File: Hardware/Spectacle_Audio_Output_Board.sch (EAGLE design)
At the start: 77 parts, among them J3 Audio Jack, J4 AUDIO-JACK3, J5 AUDIO-JACK3, U1 CY8C4146LQI-S422, U2 3.3V, U3 3.3V, U4 AT25SF041-SOIC8, Y1 12MHz

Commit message: Submitted for review by QC
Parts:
- added C11: 10uF, SparkFun-Capacitors:10UF-6.3V-20%(0603)
- added FD5, FD6, FD7, FD8: FIDUCIALUFIDUCIAL, SparkFun-Aesthetics:FIDUCIALUFIDUCIAL
- added R2: 1M, SparkFun-Resistors:1MOHM-1/10W-1%(0603)
- J3: value Audio Jack -> (none); device SparkFun-Connectors:AUDIO-JACKSMD -> SparkFun-Connectors:AUDIO-JACKSMD2
- renumbered U$2 to U5
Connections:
- new net VCCIO: C12.1, R11.2, R12.2, R13.2, R14.2, R15.2, R16.2, R17.2, R29.2, U5.IOVDD1, U5.IOVDD2, U5.IOVDD3
- new net VDDA: C11.1, U5.AVDD1, U5.AVDD2, U5.AVDD3, U5.AVDD4
- net 3.3V: now also C21.2; no longer C12.1, R11.2, R12.2, R13.2, R14.2, R15.2, R16.2, R17.2, R26.1, R29.2, U5.AVDD1, U5.AVDD2, U5.AVDD3, U5.AVDD4, U5.IOVDD1, U5.IOVDD2, U5.IOVDD3
- net GND: now also C11.2, R2.2, R26.2; no longer C21.1
- net N$12: now also R2.1
- net N$15: now also C21.1, R26.1; no longer C21.2, R26.2
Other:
- note added: "4.5V < VIN < 5.5V"
- note added: "I2C Pullup Disable"
- moved on the sheet: C21, J3, R26

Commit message: Fixes from QC review
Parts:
- renumbered C22 to C20, D5 to D1
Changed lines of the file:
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@@
 <part name="D4" library="SparkFun-DiscreteSemi" deviceset="PESD1CAN" device=""/>
 <part name="GND4" library="SparkFun-Aesthetics" deviceset="GND" device=""/>
-<part name="D5" library="SparkFun-DiscreteSemi" deviceset="PESD1CAN" device=""/>
+<part name="D1" library="SparkFun-DiscreteSemi" deviceset="PESD1CAN" device=""/>
 <part name="SUPPLY1" library="SparkFun-Aesthetics" deviceset="3.3V" device=""/>
 <part name="H1" library="SparkFun-Electromechanical" deviceset="STAND-OFF" device=""/>
@@
 <part name="GND28" library="SparkFun-Aesthetics" deviceset="GND" device=""/>
 <part name="R29" library="SparkFun-Resistors" deviceset="100KOHM-1/16W-1%(0402)" device="" value="100K"/>
-<part name="C22" library="SparkFun-Capacitors" deviceset="2.2UF-10V-20%(0603)" device="" value="2.2uF"/>
+<part name="C20" library="SparkFun-Capacitors" deviceset="2.2UF-10V-20%(0603)" device="" value="2.2uF"/>
 <part name="C12" library="SparkFun-Capacitors" deviceset="10UF-6.3V-20%(0603)" device="" value="10uF"/>
 <part name="C9" library="SparkFun-Capacitors" deviceset="0.1UF-16V(+-10%)(0402)" device="" value="0.1uF"/>
@@
 <instance part="D4" gate="G$1" x="223.52" y="71.12" rot="MR180"/>
 <instance part="GND4" gate="1" x="241.3" y="40.64"/>
-<instance part="D5" gate="G$1" x="223.52" y="43.18"/>
+<instance part="D1" gate="G$1" x="223.52" y="43.18"/>
 <instance part="SUPPLY1" gate="G$1" x="22.86" y="177.8"/>
 <instance part="H1" gate="G$1" x="246.38" y="33.02"/>
@@
 <wire x1="238.76" y1="66.04" x2="241.3" y2="66.04" width="0.1524" layer="91"/>
 <wire x1="241.3" y1="66.04" x2="241.3" y2="48.26" width="0.1524" layer="91"/>
-<pinref part="D5" gate="G$1" pin="3"/>
+<pinref part="D1" gate="G$1" pin="3"/>
 <wire x1="241.3" y1="48.26" x2="241.3" y2="43.18" width="0.1524" layer="91"/>
 <wire x1="238.76" y1="48.26" x2="241.3" y2="48.26" width="0.1524" layer="91"/>
@@
 <wire x1="208.28" y1="45.72" x2="208.28" y2="48.26" width="0.1524" layer="91"/>
 <junction x="208.28" y="71.12"/>
-<pinref part="D5" gate="G$1" pin="2"/>
+<pinref part="D1" gate="G$1" pin="2"/>
 <wire x1="208.28" y1="48.26" x2="208.28" y2="71.12" width="0.1524" layer="91"/>
 <wire x1="208.28" y1="45.72" x2="218.44" y2="45.72" width="0.1524" layer="91"/>
@@
 <attribute name="VALUE" x="80.01" y="170.942" size="1.778" layer="96" rot="R180"/>
 </instance>
-<instance part="C22" gate="G$1" x="154.94" y="165.1"/>
+<instance part="C20" gate="G$1" x="154.94" y="165.1"/>
 <instance part="C12" gate="G$1" x="213.36" y="152.4"/>
 <instance part="C9" gate="G$1" x="223.52" y="152.4"/>
@@
 <pinref part="GND22" gate="1" pin="GND"/>
 <wire x1="154.94" y1="160.02" x2="154.94" y2="162.56" width="0.1524" layer="91"/>
-<pinref part="C22" gate="G$1" pin="2"/>
+<pinref part="C20" gate="G$1" pin="2"/>
 </segment>
 <segment>
@@
 <wire x1="154.94" y1="172.72" x2="152.4" y2="172.72" width="0.1524" layer="91"/>
 <junction x="152.4" y="172.72"/>
-<pinref part="C22" gate="G$1" pin="1"/>
-</segment>
-<segment>
+<pinref part="C20" gate="G$1" pin="1"/>
+</segment>
+<segment>

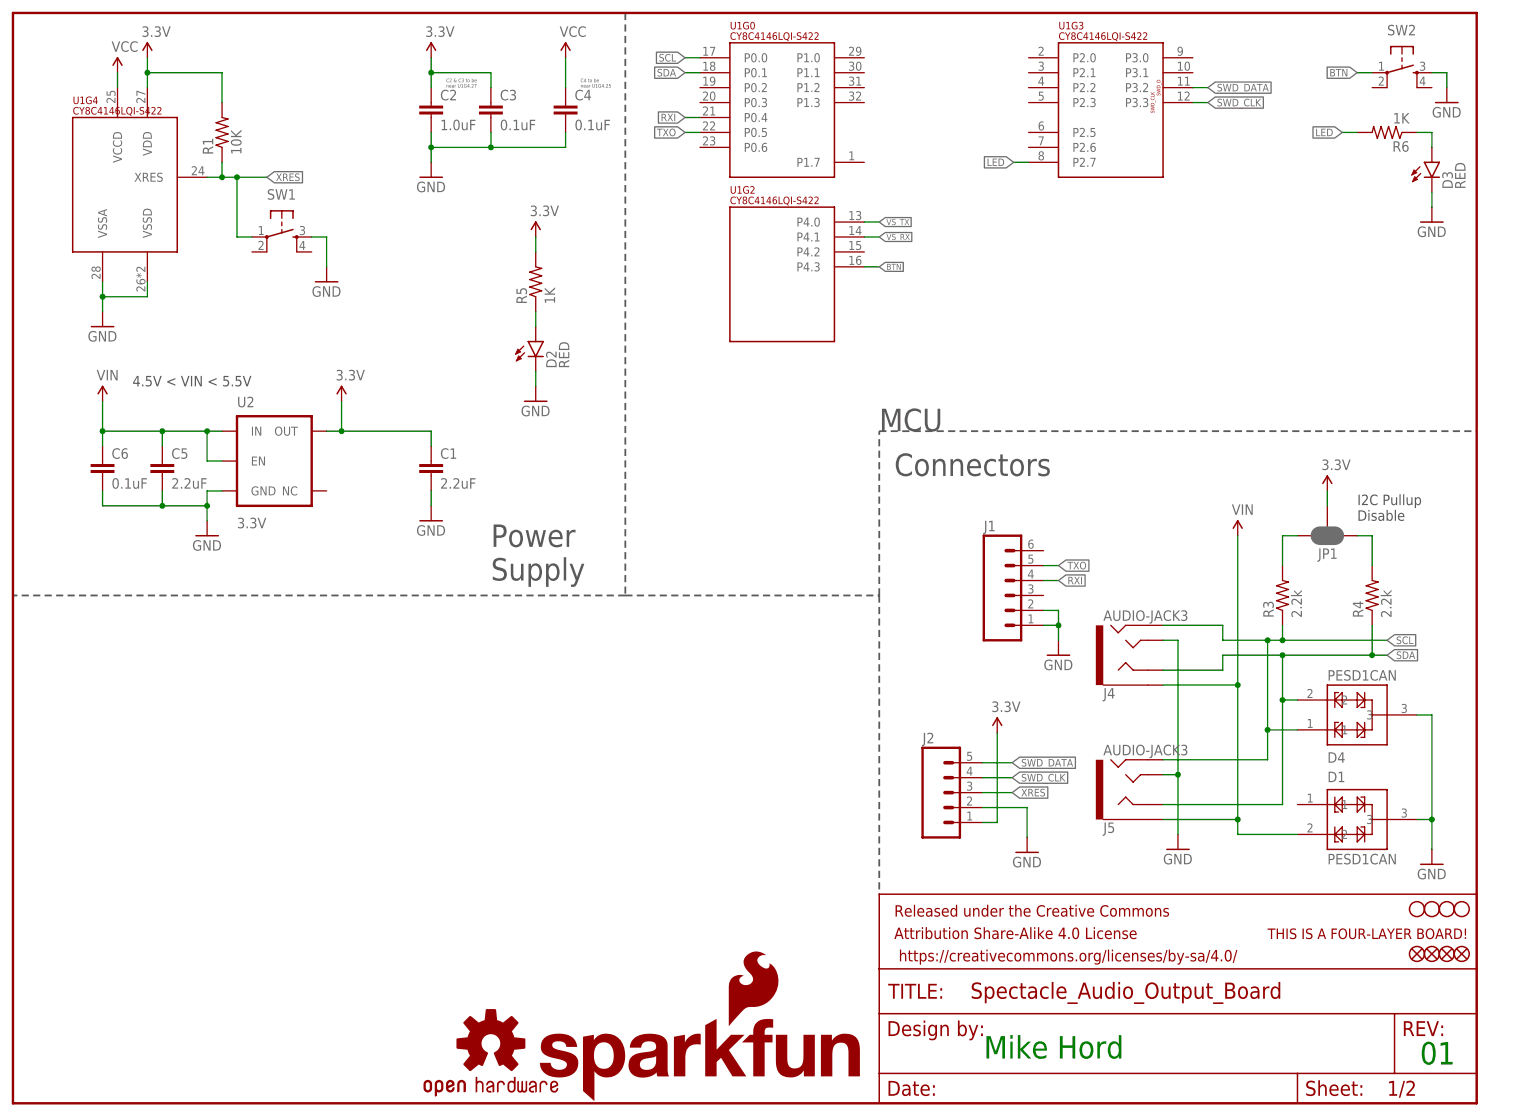
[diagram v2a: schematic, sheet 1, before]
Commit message: Added downstream power control circuitry
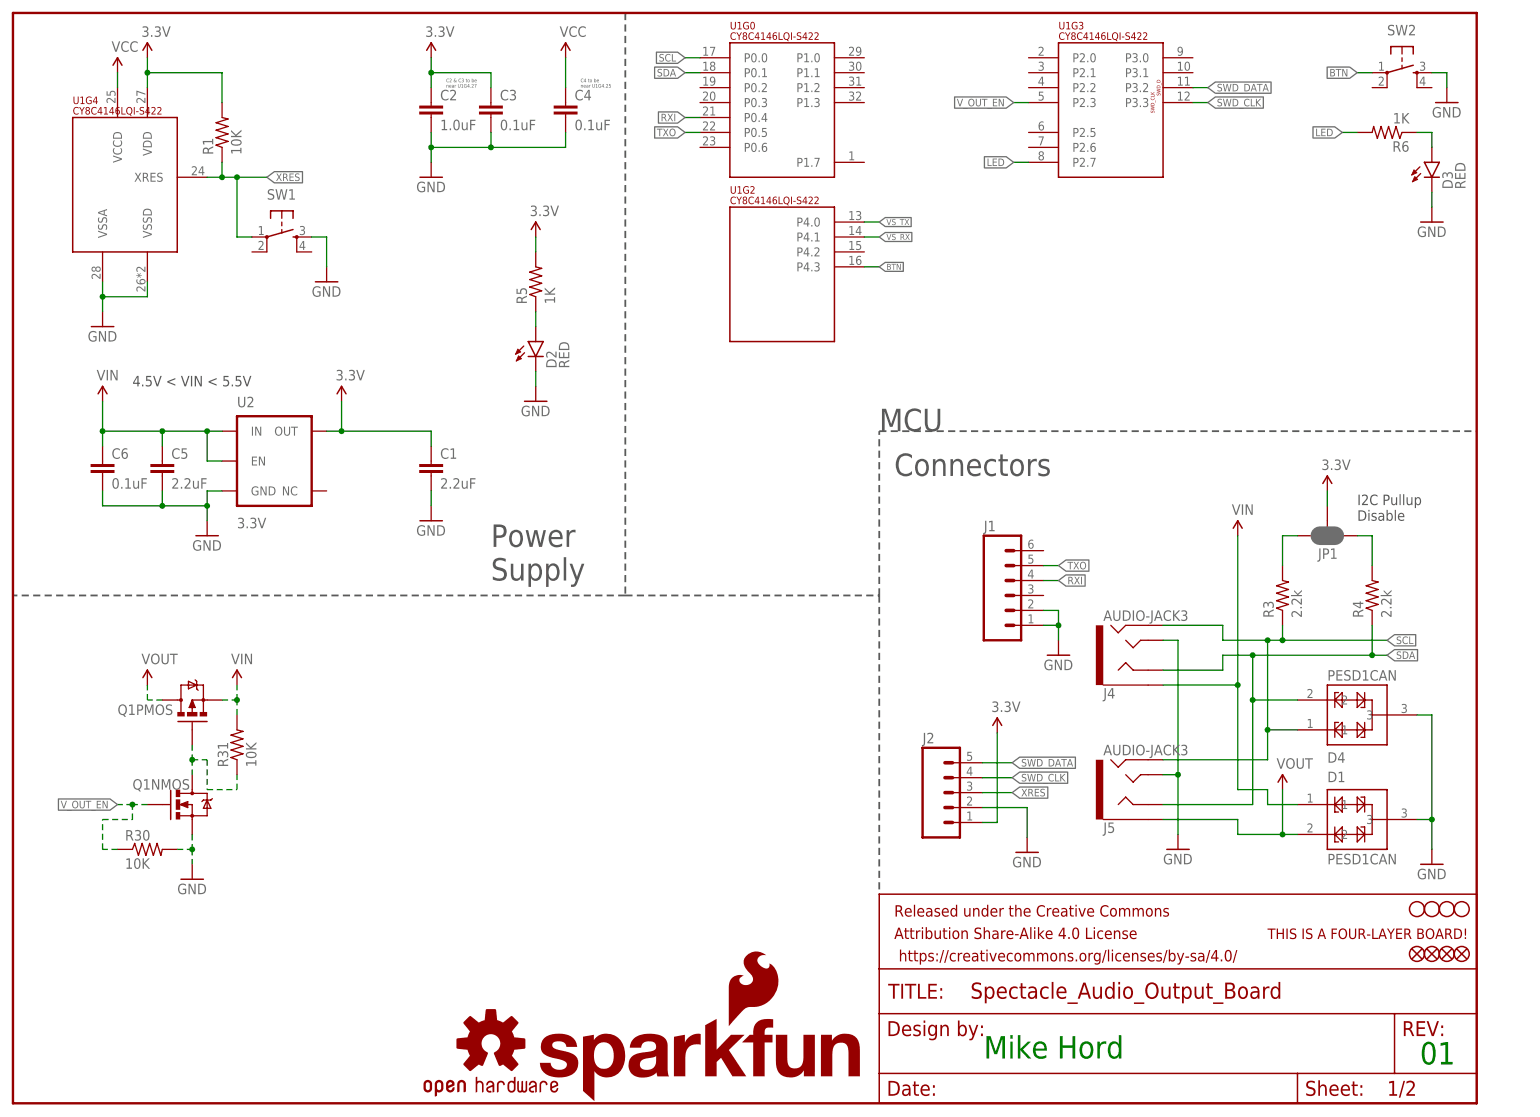
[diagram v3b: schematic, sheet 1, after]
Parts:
- added Q1: (no value), SparkFun-DiscreteSemi:IRF7509
- added R30, R31: 10K, SparkFun-Resistors:10KOHM-1/10W-1%(0603)0603
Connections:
- new net N$26: Q1NMOS.D, Q1PMOS.G, R31.1
- new net VOUT: D1.2, J5.EARTH, Q1PMOS.D
- new net V_OUT_EN: Q1NMOS.G, R30.1, U1G3.P2.3
- net GND: now also Q1NMOS.S, R30.2
- net VIN: now also D1.1, Q1PMOS.S, R31.2; no longer D1.2, J5.EARTH
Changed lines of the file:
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@@
 <part name="FD7" library="SparkFun-Aesthetics" deviceset="FIDUCIAL" device="UFIDUCIAL"/>
 <part name="FD8" library="SparkFun-Aesthetics" deviceset="FIDUCIAL" device="UFIDUCIAL"/>
+<part name="Q1" library="SparkFun-DiscreteSemi" deviceset="IRF7509" device=""/>
+<part name="GND30" library="SparkFun-Aesthetics" deviceset="GND" device=""/>
+<part name="SUPPLY23" library="SparkFun-Aesthetics" deviceset="VIN" device=""/>
+<part name="U$2" library="SparkFun-Aesthetics" deviceset="VOUT" device=""/>
+<part name="R30" library="SparkFun-Resistors" deviceset="10KOHM-1/10W-1%(0603)" device="0603" value="10K"/>
+<part name="R31" library="SparkFun-Resistors" deviceset="10KOHM-1/10W-1%(0603)" device="0603" value="10K"/>
+<part name="U$5" library="SparkFun-Aesthetics" deviceset="VOUT" device=""/>
 </parts>
 <sheets>
@@
 <instance part="FD7" gate="G$1" x="243.84" y="25.4"/>
 <instance part="FD8" gate="G$1" x="246.38" y="25.4"/>
+<instance part="Q1" gate="NMOS" x="30.48" y="50.8" smashed="yes">
+<attribute name="NAME" x="20.32" y="53.34" size="1.778" layer="95"/>
+<attribute name="VALUE" x="35.56" y="50.8" size="1.778" layer="96"/>
+</instance>
+<instance part="Q1" gate="PMOS" x="30.48" y="68.58" smashed="yes" rot="R90">
+<attribute name="NAME" x="17.78" y="66.04" size="1.778" layer="95"/>
+<attribute name="VALUE" x="30.48" y="73.66" size="1.778" layer="96" rot="R90"/>
+</instance>
+<instance part="GND30" gate="1" x="30.48" y="38.1"/>
+<instance part="SUPPLY23" gate="G$1" x="38.1" y="71.12"/>
+<instance part="U$2" gate="G$1" x="22.86" y="71.12"/>
+<instance part="R30" gate="G$1" x="22.86" y="43.18"/>
+<instance part="R31" gate="G$1" x="38.1" y="60.96" rot="R90"/>
+<instance part="U$5" gate="G$1" x="215.9" y="53.34"/>
 </instances>
 <busses>
@@
 <wire x1="238.76" y1="48.26" x2="241.3" y2="48.26" width="0.1524" layer="91"/>
 <junction x="241.3" y="48.26"/>
+</segment>
+<segment>
+<pinref part="Q1" gate="NMOS" pin="S"/>
+<pinref part="GND30" gate="1" pin="GND"/>
+<wire x1="30.48" y1="45.72" x2="30.48" y2="43.18" width="0.1524" layer="91" style="longdash"/>
+<pinref part="R30" gate="G$1" pin="2"/>
+<wire x1="30.48" y1="43.18" x2="30.48" y2="40.64" width="0.1524" layer="91" style="longdash"/>
+<wire x1="27.94" y1="43.18" x2="30.48" y2="43.18" width="0.1524" layer="91" style="longdash"/>
+<junction x="30.48" y="43.18"/>
 </segment>
 </net>
@@
 <wire x1="208.28" y1="71.12" x2="208.28" y2="96.52" width="0.1524" layer="91"/>
 <pinref part="J4" gate="G$1" pin="EARTH"/>
-<wire x1="208.28" y1="45.72" x2="208.28" y2="48.26" width="0.1524" layer="91"/>
+<wire x1="208.28" y1="71.12" x2="208.28" y2="53.34" width="0.1524" layer="91"/>
 <junction x="208.28" y="71.12"/>
-<pinref part="D1" gate="G$1" pin="2"/>
-<wire x1="208.28" y1="48.26" x2="208.28" y2="71.12" width="0.1524" layer="91"/>
-<wire x1="208.28" y1="45.72" x2="218.44" y2="45.72" width="0.1524" layer="91"/>
-<pinref part="J5" gate="G$1" pin="EARTH"/>
-<wire x1="195.58" y1="48.26" x2="208.28" y2="48.26" width="0.1524" layer="91"/>
-<junction x="208.28" y="48.26"/>
+<wire x1="208.28" y1="53.34" x2="213.36" y2="53.34" width="0.1524" layer="91"/>
+<wire x1="213.36" y1="53.34" x2="213.36" y2="50.8" width="0.1524" layer="91"/>
+<pinref part="D1" gate="G$1" pin="1"/>
+<wire x1="213.36" y1="50.8" x2="218.44" y2="50.8" width="0.1524" layer="91"/>
+</segment>
+<segment>
+<pinref part="Q1" gate="PMOS" pin="S"/>
+<wire x1="35.56" y1="68.58" x2="38.1" y2="68.58" width="0.1524" layer="91" style="longdash"/>
+<wire x1="38.1" y1="68.58" x2="38.1" y2="71.12" width="0.1524" layer="91" style="longdash"/>
+<pinref part="SUPPLY23" gate="G$1" pin="VIN"/>
+<pinref part="R31" gate="G$1" pin="2"/>
+<wire x1="38.1" y1="66.04" x2="38.1" y2="68.58" width="0.1524" layer="91" style="longdash"/>
+<junction x="38.1" y="68.58"/>
 </segment>
 </net>
@@
 <pinref part="R4" gate="G$1" pin="1"/>
 <wire x1="231.14" y1="81.28" x2="231.14" y2="76.2" width="0.1524" layer="91"/>
-<wire x1="231.14" y1="76.2" x2="215.9" y2="76.2" width="0.1524" layer="91"/>
-<wire x1="215.9" y1="76.2" x2="205.74" y2="76.2" width="0.1524" layer="91"/>
+<wire x1="231.14" y1="76.2" x2="210.82" y2="76.2" width="0.1524" layer="91"/>
+<wire x1="210.82" y1="76.2" x2="205.74" y2="76.2" width="0.1524" layer="91"/>
 <wire x1="231.14" y1="76.2" x2="233.68" y2="76.2" width="0.1524" layer="91"/>
 <junction x="231.14" y="76.2"/>
@@
 <pinref part="J4" gate="G$1" pin="RING1"/>
 <wire x1="205.74" y1="73.66" x2="195.58" y2="73.66" width="0.1524" layer="91"/>
-<wire x1="215.9" y1="68.58" x2="215.9" y2="76.2" width="0.1524" layer="91"/>
-<junction x="215.9" y="76.2"/>
+<wire x1="210.82" y1="68.58" x2="210.82" y2="76.2" width="0.1524" layer="91"/>
+<junction x="210.82" y="76.2"/>
 <pinref part="D4" gate="G$1" pin="2"/>
-<wire x1="218.44" y1="68.58" x2="215.9" y2="68.58" width="0.1524" layer="91"/>
+<wire x1="218.44" y1="68.58" x2="210.82" y2="68.58" width="0.1524" layer="91"/>
 <pinref part="J5" gate="G$1" pin="RING1"/>
-<wire x1="195.58" y1="50.8" x2="215.9" y2="50.8" width="0.1524" layer="91"/>
-<wire x1="215.9" y1="50.8" x2="215.9" y2="68.58" width="0.1524" layer="91"/>
-<junction x="215.9" y="68.58"/>
+<wire x1="195.58" y1="50.8" x2="210.82" y2="50.8" width="0.1524" layer="91"/>
+<wire x1="210.82" y1="50.8" x2="210.82" y2="68.58" width="0.1524" layer="91"/>
+<junction x="210.82" y="68.58"/>
 </segment>
 <segment>
@@
 </segment>
 </net>
+<net name="N$26" class="0">
+<segment>
+<pinref part="Q1" gate="PMOS" pin="G"/>
+<pinref part="Q1" gate="NMOS" pin="D"/>
+<wire x1="30.48" y1="60.96" x2="30.48" y2="58.42" width="0.1524" layer="91" style="longdash"/>
+<wire x1="30.48" y1="58.42" x2="30.48" y2="55.88" width="0.1524" layer="91" style="longdash"/>
+<wire x1="30.48" y1="58.42" x2="33.02" y2="58.42" width="0.1524" layer="91" style="longdash"/>
+<junction x="30.48" y="58.42"/>
+<wire x1="33.02" y1="58.42" x2="33.02" y2="53.34" width="0.1524" layer="91" style="longdash"/>
+<pinref part="R31" gate="G$1" pin="1"/>
+<wire x1="33.02" y1="53.34" x2="38.1" y2="53.34" width="0.1524" layer="91" style="longdash"/>
+<wire x1="38.1" y1="53.34" x2="38.1" y2="55.88" width="0.1524" layer="91" style="longdash"/>
+</segment>
+</net>
+<net name="VOUT" class="0">
+<segment>
+<pinref part="Q1" gate="PMOS" pin="D"/>
+<wire x1="25.4" y1="68.58" x2="22.86" y2="68.58" width="0.1524" layer="91" style="longdash"/>
+<wire x1="22.86" y1="68.58" x2="22.86" y2="71.12" width="0.1524" layer="91" style="longdash"/>
+<pinref part="U$2" gate="G$1" pin="VOUT"/>
+</segment>
+<segment>
+<pinref part="D1" gate="G$1" pin="2"/>
+<pinref part="J5" gate="G$1" pin="EARTH"/>
+<wire x1="195.58" y1="48.26" x2="208.28" y2="48.26" width="0.1524" layer="91"/>
+<wire x1="208.28" y1="45.72" x2="208.28" y2="48.26" width="0.1524" layer="91"/>
+<wire x1="208.28" y1="45.72" x2="215.9" y2="45.72" width="0.1524" layer="91"/>
+<pinref part="U$5" gate="G$1" pin="VOUT"/>
+<wire x1="215.9" y1="45.72" x2="218.44" y2="45.72" width="0.1524" layer="91"/>
+<wire x1="215.9" y1="53.34" x2="215.9" y2="45.72" width="0.1524" layer="91"/>
+<junction x="215.9" y="45.72"/>
+</segment>
+</net>
+<net name="V_OUT_EN" class="0">
+<segment>
+<pinref part="Q1" gate="NMOS" pin="G"/>
+<wire x1="22.86" y1="50.8" x2="20.32" y2="50.8" width="0.1524" layer="91" style="longdash"/>
+<label x="17.78" y="50.8" size="1.27" layer="95" rot="R180" xref="yes"/>
+<pinref part="R30" gate="G$1" pin="1"/>
+<wire x1="20.32" y1="50.8" x2="17.78" y2="50.8" width="0.1524" layer="91" style="longdash"/>
+<wire x1="17.78" y1="43.18" x2="15.24" y2="43.18" width="0.1524" layer="91" style="longdash"/>
+<wire x1="15.24" y1="43.18" x2="15.24" y2="48.26" width="0.1524" layer="91" style="longdash"/>
+<wire x1="15.24" y1="48.26" x2="20.32" y2="48.26" width="0.1524" layer="91" style="longdash"/>
+<wire x1="20.32" y1="48.26" x2="20.32" y2="50.8" width="0.1524" layer="91" style="longdash"/>
+<junction x="20.32" y="50.8"/>
+</segment>
+<segment>
+<pinref part="U1" gate="G3" pin="P2.3"/>
+<wire x1="172.72" y1="170.18" x2="170.18" y2="170.18" width="0.1524" layer="91"/>
+<label x="170.18" y="170.18" size="1.27" layer="95" rot="R180" xref="yes"/>
+</segment>
+</net>
